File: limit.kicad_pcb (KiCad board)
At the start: 2 copper layers, 15.2 x 17 mm, 6 parts, among them P0 GP1S093HCZ0F

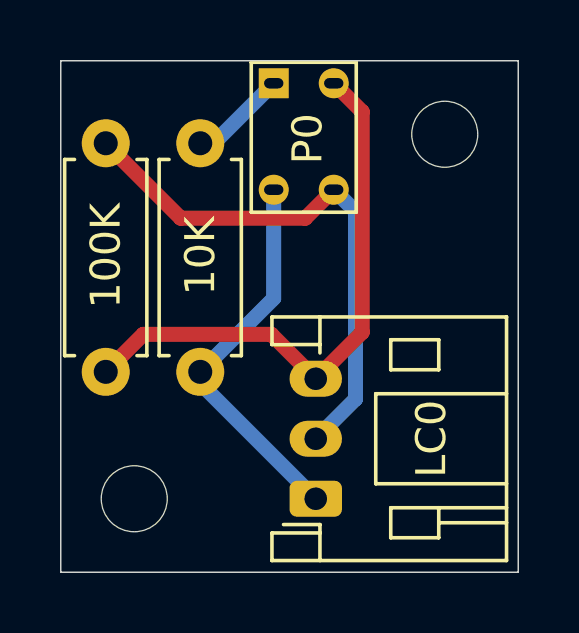
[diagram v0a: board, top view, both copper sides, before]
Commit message: resistance changed from 10K to 1K ohms
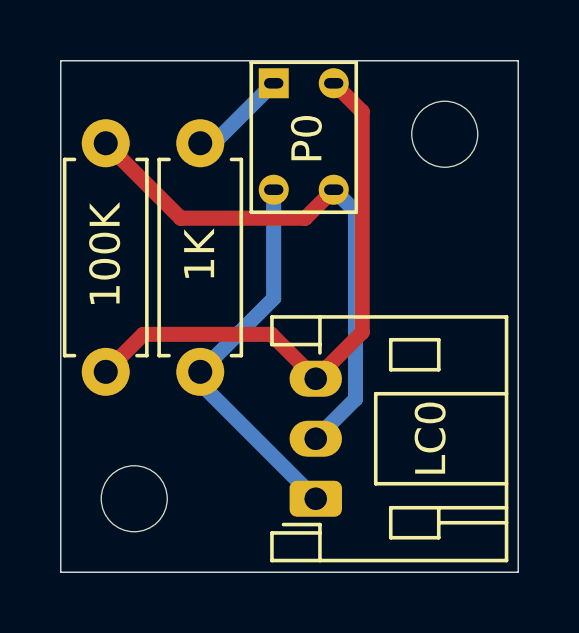
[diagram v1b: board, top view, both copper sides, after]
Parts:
- R1: value 10K -> 1K
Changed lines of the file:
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@@
   )
   (setup
-    (last_trace_width 0.5)
+    (last_trace_width 0.25)
     (user_trace_width 0.5)
     (trace_clearance 0.2)
@@
       (effects (font (size 1 1) (thickness 0.15)))
     )
-    (fp_text value 10K (at 3.75 0 90) (layer F.SilkS)
+    (fp_text value 1K (at 3.75 0 90) (layer F.SilkS)
       (effects (font (size 1 1) (thickness 0.15)))
     )
